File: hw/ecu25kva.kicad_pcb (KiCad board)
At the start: 4 copper layers, 180 x 130 mm, 379 parts, among them J1001 CONN_ECU_94, J301 SWD/JTAG, Q101 SQD50P08-25L, Q102 IPD90N10S4-06, Q103 SQM120P10-10m1L, Q104 SQM120P10-10m1L, Q201 IPD90N10S4-06, Q301 2N7002BK, Q401 DMN15H310SK3, Q402 2N7002BK, Q403 2N7002BK, Q404 2N7002BK, Q405 2N7002BK, Q406 PZTA42-Q, Q407 PMBT3904-Q, Q408 SQM85N15-19, Q409 IPD90N10S4-06, Q410 SQM85N15-19, Q411 IPD90N10S4-06, Q412 SQM85N15-19, Q413 2N7002BK, Q414 SQM85N15-19, Q415 2N7002BK, Q416 SQM85N15-19, Q417 2N7002BK, Q418 PZTA42-Q, Q419 PMBT3904-Q, Q501 IPD90N10S4-06, Q502 2N7002BK, Q503 IPD90N10S4-06, Q504 IPD90N10S4-06, Q505 IPD90N10S4-06, Q506 IPD90N10S4-06, Q507 2N7002BK, Q801 PMBT3904-Q, Q802 PMBT3904-Q, Q803 PMBT3904-Q, Q804 PMBT3904-Q, Q805 PMBT3904-Q, Q806 PMV280ENEA, Q807 PMV280ENEA, U101 TLV3201, U102 UCC27517A, U201 LM5164, U202 TLV76733, U203 TPS48110, U204 TPS7B4253, U205 TPS7B4253, U206 TPS7B4253, U301 S32K148_144LQFP, U302 TPS3850G33, U401 TPS40210, U402 AUIRS2181S, U403 AUIRS2181S, U404 AUIRS2181S, U405 AUIRS2181S, U406 INA181A1, U407 INA181A1, U501 INA181A1, U502 AUIRS2181S, U503 INA181A1, U504 AUIRS2184S, U505 AUIRS2184S, U601 INA592, U602 INA592, U603 INA592, U604 INA592, U605 INA592, U606 MPXHZ6115A, U701 TLV3201, U801 SN74AHCT1G125-Q1, U802 SN74AHCT1G125-Q1, U901 TCAN1042HGV, U902 TCAN1042HGV

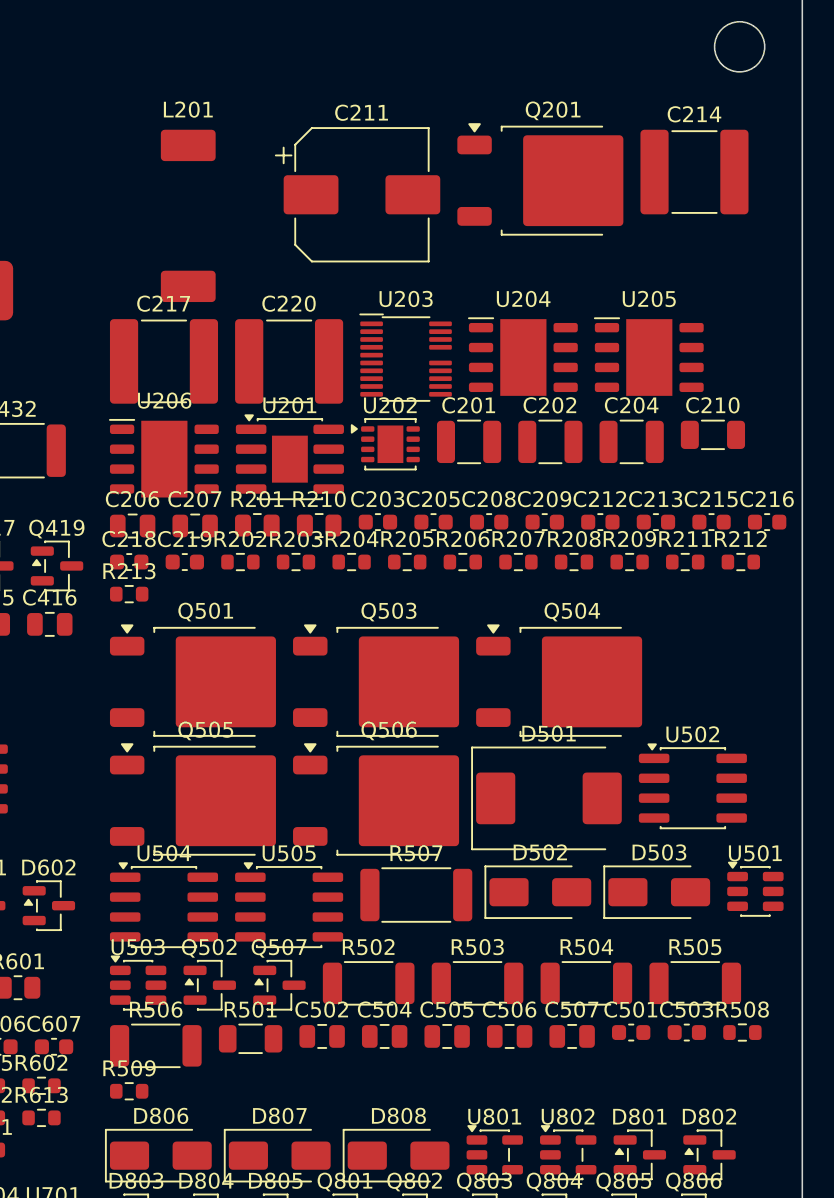
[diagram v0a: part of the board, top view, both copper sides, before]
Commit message: PCB review fixes: shorts and parity fail the check, fine-pitch and fused-feed classes, linked footprints
- check_pcb fails on every DRC error and on schematic parity
- footprints carry their schematic path and fields; net names match the schematic's
- 3V3/5V/boost-controller nets and shunt tops at 0.15 mm; pin-6 EGR feed sized for its 10 A loom fuse; EGR high-side gates at 0.6 mm
- metering/EGR block moved into the contact band
- layout guide: Q101/Q102 gate drive corrected, heat rules for Q103/Q104 and the EGR bridge
- brief 6.3: pitch measured over ten gaps
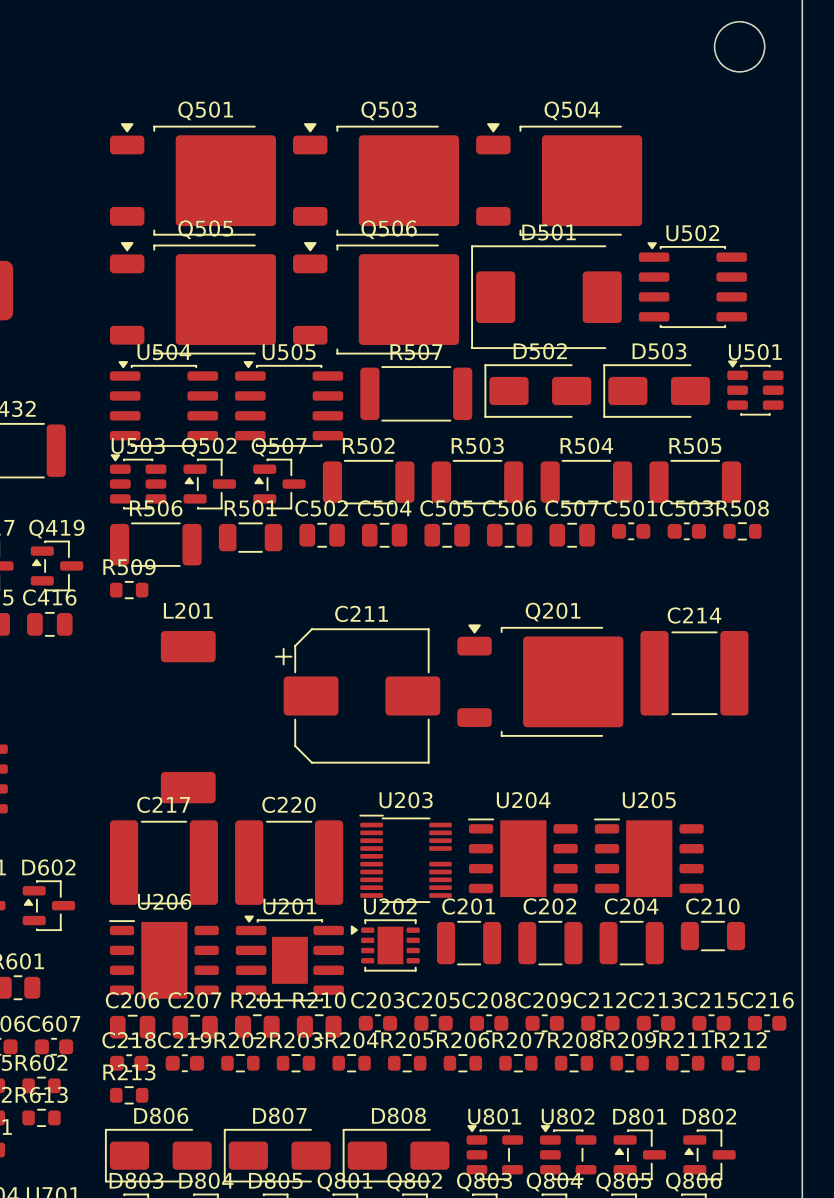
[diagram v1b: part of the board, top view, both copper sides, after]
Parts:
- moved C210 32.0 mm to (194.3, 80.8)
- moved Q502 32.0 mm to (162.2, 51.9)
- moved Q505 32.0 mm to (161.9, 40.1)
- moved Q506 32.0 mm to (173.6, 40.1)
- moved Q507 32.0 mm to (166.6, 51.9)
- moved U503 32.0 mm to (157.6, 51.9)
- moved C203 32.0 mm to (172.9, 86.3)
- moved C205 32.0 mm to (176.5, 86.3)
- moved C206 32.0 mm to (157.2, 86.6)
- moved C207 32.0 mm to (161.2, 86.6)
- moved C208 32.0 mm to (180.0, 86.3)
- moved C209 32.0 mm to (183.6, 86.3)
- moved C212 32.0 mm to (187.1, 86.3)
- moved C213 32.0 mm to (190.7, 86.3)
- moved C215 32.0 mm to (194.2, 86.3)
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
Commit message: Separate the supervisor's RESET and WDO nets: their pullups overlapped and shorted them
The two 10k pullups sat in one column 2.54 mm apart, and RESET's lead
wire ran through WDO's pullup pin. RESET, WDO, the MCU reset pin, the
kill inverter gate and WDT_FAULT were one net, so firmware could not
tell a watchdog trip from a rail trip. WDO's pullup now hangs below its
pin. check_netlist gains MUST_SEPARATE so it cannot come back; the
production board's seven pads were moved onto the new net in place.
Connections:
- J301 pad 10: /mcu/WDT_FAULT -> /mcu/~{RESET}
- Q301 pad 1: /mcu/WDT_FAULT -> /mcu/~{RESET}
- R301 pad 2: /mcu/WDT_FAULT -> /mcu/~{RESET}
- R302 pad 1: /3V3_MCU -> /mcu/WDT_FAULT
- R302 pad 2: /mcu/WDT_FAULT -> /3V3_MCU
- U301 pad 141: /mcu/WDT_FAULT -> /mcu/~{RESET}
- U302 pad 9: /mcu/WDT_FAULT -> /mcu/~{RESET}

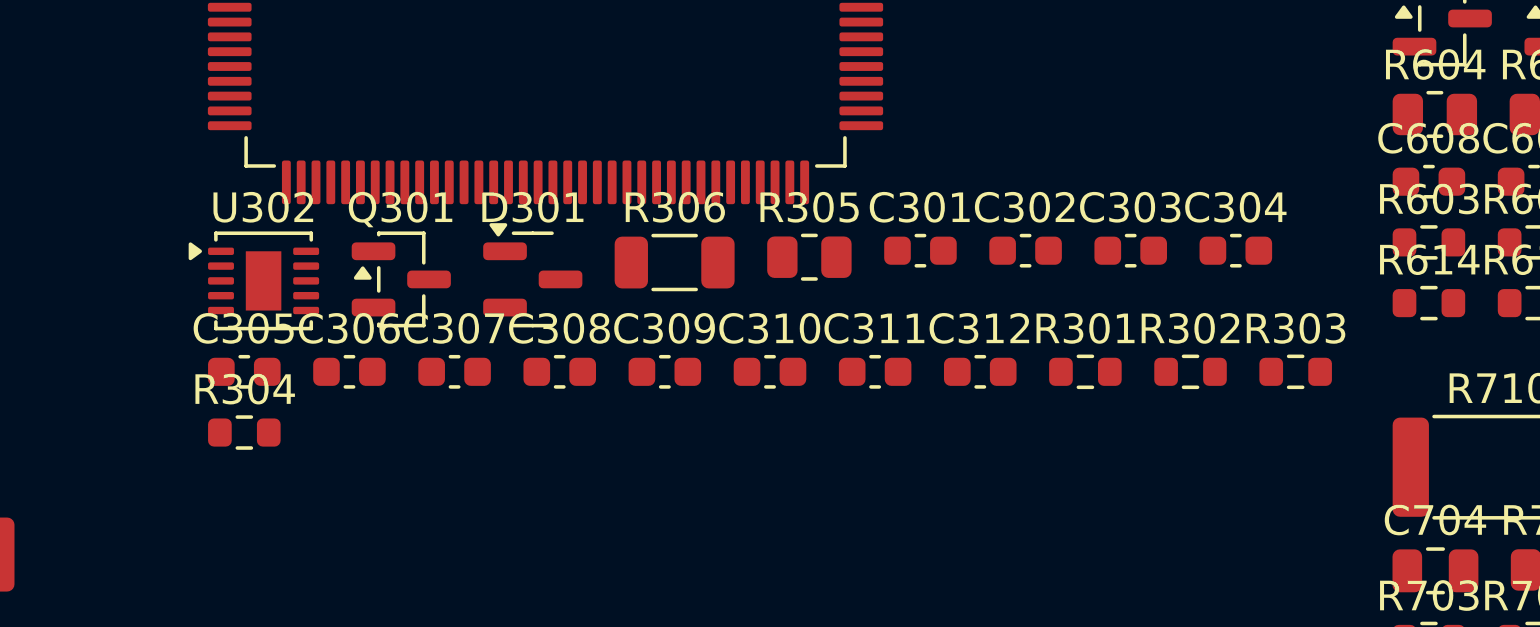
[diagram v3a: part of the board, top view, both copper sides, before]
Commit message: Prototype review fixes: watchdog kill restored, pour checks that can fail
- D302 (BAT54Q-7-F, anode ~RESET, cathode WDT_FAULT) restores the
  watchdog-to-gate-kill path the 15 Oct supervisor fix removed; production
  and prototype. check_netlist WDO_KILL guards it. WDT_FAULT no longer
  records which trip it was; docs corrected.
- gen_board: sync stage (rename shifted refs, place new parts on a routed
  board), clusters stage, rip_thin, per-net IPC targets in widen, outer-only
  routing for nets In2 cannot carry, finish undoes a pass that necks a pour.
- Tests: pour connectivity read from pcbnew (the DRC list stops at ~500),
  test_no_necks, test_track_power_widths (TRACK_AMPS), test_inputs_committed.
- The 5 V buck's output and switch node now run on the outer layers.
- check_pcb: a parity entry with no items no longer crashes it.
- bring-up guide: probe rating, charged boost caps, 5 A limit, kill FETs.
- Decisions §15, status, handoff traps; fab files and PDF rebuilt.
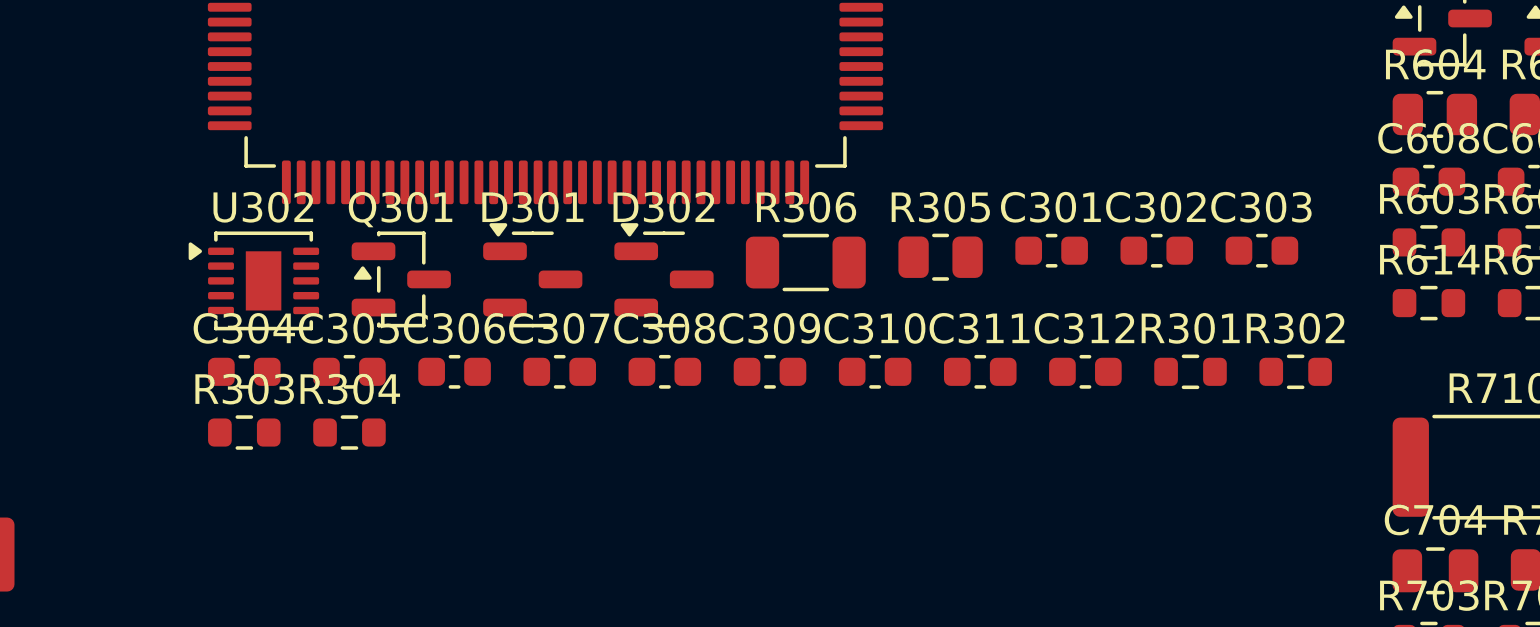
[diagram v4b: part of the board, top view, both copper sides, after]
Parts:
- added D302: BAT54Q-7-F, ecu25kva:SOT-23_Zener_K1_A2, F.Cu at (97.2, 93.6)
- moved R303 35.6 mm to (83.0, 98.8)
- moved C304 33.7 mm to (83.0, 96.8)
- moved C303 4.43 mm to (117.4, 92.7)
- moved C301 4.43 mm to (110.3, 92.7)
- moved C302 4.43 mm to (113.8, 92.7)
- moved R305 4.43 mm to (106.5, 92.9)
- moved R306 4.43 mm to (102.0, 93.1)
- moved C309 3.55 mm to (100.8, 96.8)
- moved R302 3.55 mm to (118.5, 96.8)
- moved C305 3.55 mm to (86.6, 96.8)
- moved C306 3.55 mm to (90.1, 96.8)
- moved C307 3.55 mm to (93.7, 96.8)
- moved C308 3.55 mm to (97.2, 96.8)
- moved C310 3.55 mm to (104.3, 96.8)
- moved C311 3.55 mm to (107.9, 96.8)
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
